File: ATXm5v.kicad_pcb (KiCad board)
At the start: 4 copper layers, 48.3 x 44.5 mm, 5 parts, among them J1 ATX IN, J2 ATX OUT, U1 L7905

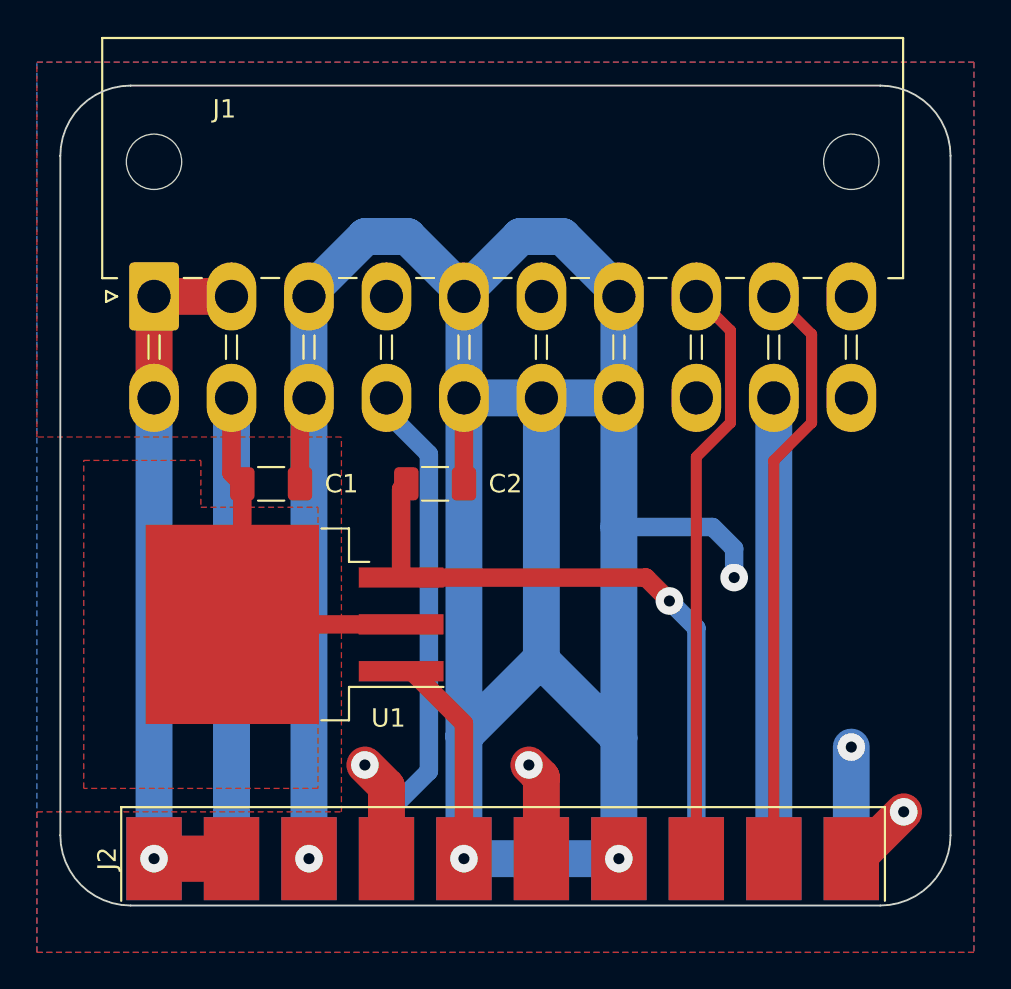
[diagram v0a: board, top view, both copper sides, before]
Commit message: Fixed connector direction
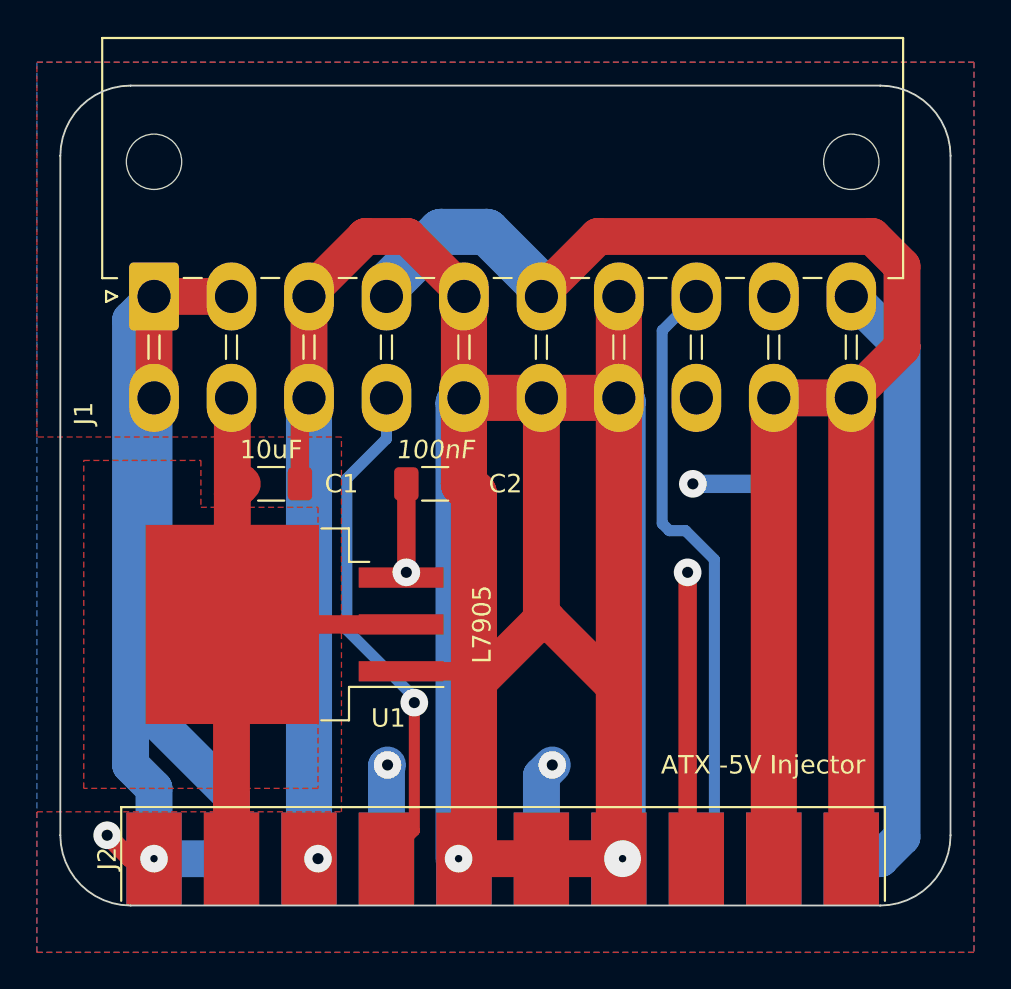
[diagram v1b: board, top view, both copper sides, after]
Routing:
- net VCC: track 192.9 -> 242.1 mm, vias 3 -> 2
- net /3.3V: track 75.6 -> 117.8 mm, vias 1 -> 2
- net /5VSB: track 32.2 -> 53.5 mm, vias 0 -> 1
- net GND: track 186.5 -> 202.3 mm, vias 4 -> 3
- net /-12V: track 46.9 -> 35.7 mm
- net /PWR_OK: track 32.0 -> 33.3 mm
- net /-5V: track 34.8 -> 36.2 mm, vias 1 -> 2
- net /~PS_ON: track 26.9 -> 28.2 mm, vias 0 -> 1
- net /+12V: track 33.0 -> 33.7 mm, vias 1 -> 0
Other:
- board text added: "ATX -5V Injector"
